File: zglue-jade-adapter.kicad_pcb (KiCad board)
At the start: 6 copper layers, 25 x 20 mm, 77 parts, among them J1 543630489, J2 543630489, U1 zGlue-Jade

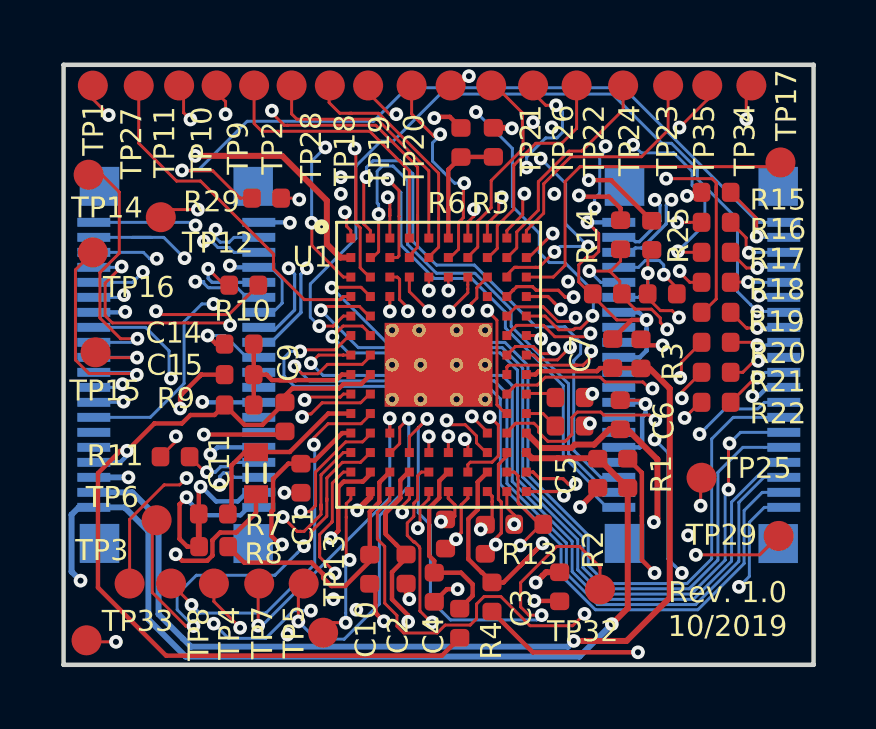
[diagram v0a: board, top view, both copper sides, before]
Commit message: Add resistors for choosing CSI_LP signals connection
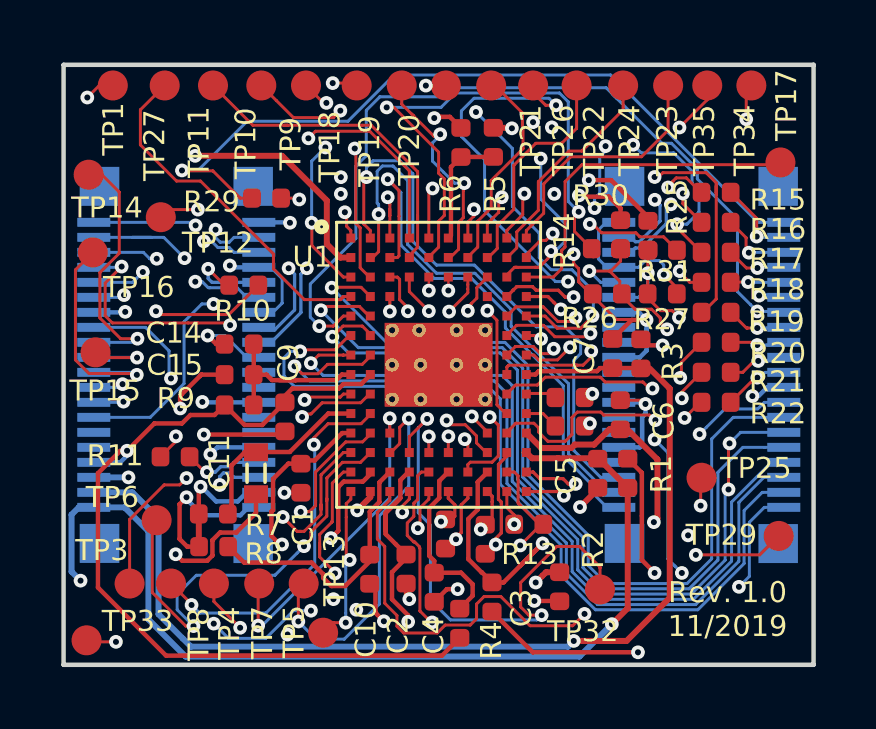
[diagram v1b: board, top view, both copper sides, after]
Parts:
- removed TP2, TP28: TP_SMD1MM, antmicro-footprints:Testpoint_smd_1mm
- added R30: R_22R_0402, antmicro-footprints:0402-res, F.Cu at (18.1, 6.13)
- added R31: R_22R_0402, antmicro-footprints:0402-res, F.Cu at (20.0, 6.18)
- moved TP9 1.73 mm to (8.08, 0.64)
- moved TP10 1.49 mm to (6.59, 0.64)
- moved TP11 1.13 mm to (4.98, 0.64)
- moved TP27 0.87 mm to (3.32, 0.69)
- moved TP1 0.67 mm to (1.64, 0.64)
- moved TP18 0.38 mm to (9.72, 0.69)
- moved TP19 0.33 mm to (11.2, 0.69)
- moved TP20 0.16 mm to (12.7, 0.69)
- moved R25 0.12 mm to (19.5, 5.68)
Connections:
- net /LP_CSI_D1_OUT_N renamed /RDL_LP_CSI_D1_OUT_N
- net /LP_CSI_D1_OUT_P renamed /RDL_LP_CSI_D1_OUT_P
- U1 pad A5: /PIO5 -> /PROG_LP_CSI_D1_OUT_N
- U1 pad B5: /PIO4 -> /PROG_LP_CSI_D1_OUT_P
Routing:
- net /PROG_LP_CSI_D1_OUT_P: track 0.00 -> 18.1 mm, vias 0 -> 2
- net /PROG_LP_CSI_D1_OUT_N: track 0.00 -> 12.4 mm, vias 0 -> 2
- net /PIO5: track 8.31 -> 0.00 mm
- net /PIO4: track 8.06 -> 0.00 mm
- net /PIO14: track 13.1 -> 16.4 mm, vias 4 -> 3
- net /PIO6: track 8.01 -> 10.6 mm
- net /PIO1: track 13.1 -> 11.3 mm, vias 2 -> 0
- net /PROC_SI: track 20.1 -> 21.7 mm
- net /PROC_SO: track 22.6 -> 24.0 mm
- net /PIO2: track 14.3 -> 12.9 mm
- net /CTRL_RST_FLASH_SOC_CS: track 27.3 -> 28.5 mm
- net Net-(TP34-Pad1): track 16.2 -> 15.1 mm, vias 4 -> 3
- net /PIO0: track 17.1 -> 17.8 mm
- net /PIO15: track 11.4 -> 11.9 mm
- net /PIO3: track 9.10 -> 8.60 mm, vias 0 -> 2
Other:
- board text added: "R26"
- board text added: "R27"
- board text added: "Rev. 1.0 11/2019"
- board text removed: "Rev. 1.0 10/2019"

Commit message: Regenerate libraries
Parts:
- C1, C10, C14, C15, C2, C3, C4, C5, C6, C7, C9: footprint antmicro-footprints:0402-cap -> zglue-jade-adapter-footprints:0402-cap
- C11: footprint antmicro-footprints:0603-cap -> zglue-jade-adapter-footprints:0603-cap
- J1, J2: footprint antmicro-footprints:543630489 -> zglue-jade-adapter-footprints:543630489
- R1, R10, R11, R12, R13, R14, R15, R16, R17, R18, R19, R2, R20, R21, R22, R23, R24, R25, R26, R27, R28, R29, R3, R30, R31, R4, R5, R6, R7, R8, R9: footprint antmicro-footprints:0402-res -> zglue-jade-adapter-footprints:0402-res
- TP1, TP10, TP11, TP12, TP13, TP14, TP15, TP16, TP17, TP18, TP19, TP20, TP21, TP22, TP23, TP24, TP25, TP26, TP27, TP29, TP3, TP32, TP33, TP34, TP35, TP4, TP5, TP6, TP7, TP8, TP9: footprint antmicro-footprints:Testpoint_smd_1mm -> zglue-jade-adapter-footprints:Testpoint_smd_1mm
- U1: footprint lib:Z-Glue_LGA-96 -> zglue-jade-adapter-footprints:Z-Glue_LGA-96
